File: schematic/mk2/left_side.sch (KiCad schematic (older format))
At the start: 7 parts

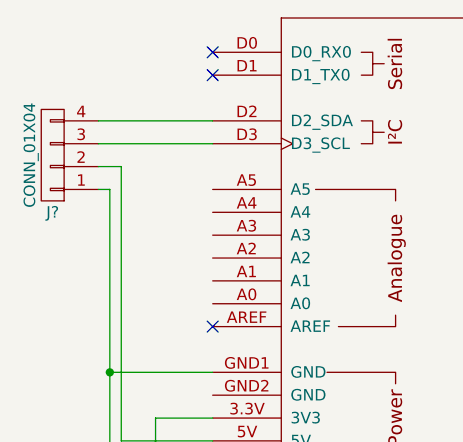
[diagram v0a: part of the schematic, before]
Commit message: schematic: Fix the hierarchical schematics and add outputs to left_side
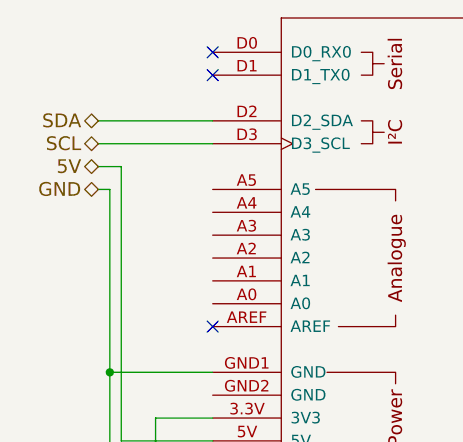
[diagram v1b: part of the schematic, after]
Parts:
- removed J?: CONN_01X04, symbol CONN_01X04
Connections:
- net 5V: now reaches ARD?.5V
- net SDA: now reaches ARD?.D2 (D2_SDA)
- net SCL: now reaches ARD?.D3 (D3_SCL)
- net GND: now reaches ARD?.GND1 (GND), J?.7 (P7)
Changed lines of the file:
@@
 LIBS:contrib
 LIBS:valves
+LIBS:left_side-cache
 EELAYER 25 0
 EELAYER END
@@
 NoConn ~ 4800 2400
 NoConn ~ 2200 2700
-$Comp
-L CONN_01X04 J?
-U 1 1 5A20AD93
-P 1500 1950
-F 0 "J?" H 1500 2200 50  0000 C CNN
-F 1 "CONN_01X04" V 1600 1950 50  0000 C CNN
-F 2 "" H 1500 1950 50  0001 C CNN
-F 3 "" H 1500 1950 50  0001 C CNN
-	1    1500 1950
-	-1   0    0    1
-$EndComp
 NoConn ~ 2200 1500
 NoConn ~ 2200 1600
@@
 Wire Wire Line
 	8750 4275 8450 4275
+Text HLabel 1700 1800 0    60   BiDi ~ 0
+SDA
+Text HLabel 1700 1900 0    60   BiDi ~ 0
+SCL
+Text HLabel 1700 2000 0    60   BiDi ~ 0
+5V
+Text HLabel 1700 2100 0    60   BiDi ~ 0
+GND
 $EndSCHEMATC
